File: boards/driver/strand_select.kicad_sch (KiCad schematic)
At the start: 16 parts, among them Q89 MMBT2222, Q90 MMBT2907, Q91 MMBT2222

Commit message: Driver: minor schematic cleanup and populated all of the BOM except for resistors
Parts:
- D158, D159, D160, D161, D162: MPN (none) -> 1N4148WS; Manufacturer (none) -> SMC Diode Solutions; Package (none) -> SOD-323; Rating (none) -> 300mA
- Q89, Q91: MPN (none) -> MMBT2222ALT1HTSA1; Manufacturer (none) -> Infineon Technologies; Package (none) -> SOT-23-3
- Q90: MPN (none) -> MMBT2907ALT1HTSA1; Manufacturer (none) -> Infineon Technologies; Package (none) -> SOT-23-3
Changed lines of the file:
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@@
+      (effects (font (size 1.27 1.27)) hide)
+    )
+    (property "MPN" "MMBT2907ALT1HTSA1" (id 6) (at 72.39 95.25 0)
+      (effects (font (size 1.27 1.27)) hide)
+    )
+    (property "Manufacturer" "Infineon Technologies" (id 7) (at 72.39 95.25 0)
+      (effects (font (size 1.27 1.27)) hide)
+    )
+    (property "Description" "TRANS PNP 60V 0.6A SOT23" (id 8) (at 72.39 95.25 0)
+      (effects (font (size 1.27 1.27)) hide)
+    )
+    (property "Package" "SOT-23-3" (id 9) (at 72.39 95.25 0)
       (effects (font (size 1.27 1.27)) hide)
     )
@@
       (effects (font (size 1.27 1.27)) hide)
     )
+    (property "MPN" "1N4148WS" (id 6) (at 74.93 86.36 0)
+      (effects (font (size 1.27 1.27)) hide)
+    )
+    (property "Manufacturer" "SMC Diode Solutions" (id 7) (at 74.93 86.36 0)
+      (effects (font (size 1.27 1.27)) hide)
+    )
+    (property "Description" "DIODE GEN PURP 75V 300MA SOD323" (id 8) (at 74.93 86.36 0)
+      (effects (font (size 1.27 1.27)) hide)
+    )
+    (property "Package" "SOD-323" (id 9) (at 74.93 86.36 0)
+      (effects (font (size 1.27 1.27)) hide)
+    )
+    (property "Rating" "300mA" (id 10) (at 74.93 86.36 0)
+      (effects (font (size 1.27 1.27)) hide)
+    )
     (pin "1")
     (pin "2")
@@
       (effects (font (size 1.27 1.27)) hide)
     )
+    (property "MPN" "1N4148WS" (id 6) (at 86.36 115.57 0)
+      (effects (font (size 1.27 1.27)) hide)
+    )
+    (property "Manufacturer" "SMC Diode Solutions" (id 7) (at 86.36 115.57 0)
+      (effects (font (size 1.27 1.27)) hide)
+    )
+    (property "Description" "DIODE GEN PURP 75V 300MA SOD323" (id 8) (at 86.36 115.57 0)
+      (effects (font (size 1.27 1.27)) hide)
+    )
+    (property "Package" "SOD-323" (id 9) (at 86.36 115.57 0)
+      (effects (font (size 1.27 1.27)) hide)
+    )
+    (property "Rating" "300mA" (id 10) (at 86.36 115.57 0)
+      (effects (font (size 1.27 1.27)) hide)
+    )
     (pin "1")
     (pin "2")
@@
       (effects (font (size 1.27 1.27)) hide)
     )
+    (property "MPN" "1N4148WS" (id 6) (at 86.36 121.92 0)
+      (effects (font (size 1.27 1.27)) hide)
+    )
+    (property "Manufacturer" "SMC Diode Solutions" (id 7) (at 86.36 121.92 0)
+      (effects (font (size 1.27 1.27)) hide)
+    )
+    (property "Description" "DIODE GEN PURP 75V 300MA SOD323" (id 8) (at 86.36 121.92 0)
+      (effects (font (size 1.27 1.27)) hide)
+    )
+    (property "Package" "SOD-323" (id 9) (at 86.36 121.92 0)
+      (effects (font (size 1.27 1.27)) hide)
+    )
+    (property "Rating" "300mA" (id 10) (at 86.36 121.92 0)
+      (effects (font (size 1.27 1.27)) hide)
+    )
     (pin "1")
     (pin "2")
@@
       (effects (font (size 1.27 1.27)) hide)
     )
+    (property "MPN" "1N4148WS" (id 6) (at 86.36 128.27 0)
+      (effects (font (size 1.27 1.27)) hide)
+    )
+    (property "Manufacturer" "SMC Diode Solutions" (id 7) (at 86.36 128.27 0)
+      (effects (font (size 1.27 1.27)) hide)
+    )
+    (property "Description" "DIODE GEN PURP 75V 300MA SOD323" (id 8) (at 86.36 128.27 0)
+      (effects (font (size 1.27 1.27)) hide)
+    )
+    (property "Package" "SOD-323" (id 9) (at 86.36 128.27 0)
+      (effects (font (size 1.27 1.27)) hide)
+    )
+    (property "Rating" "300mA" (id 10) (at 86.36 128.27 0)
+      (effects (font (size 1.27 1.27)) hide)
+    )
     (pin "1")
     (pin "2")
@@
     )
     (property "Part Number" "MMBT2222A-G" (id 5) (at 99.06 110.49 0)
+      (effects (font (size 1.27 1.27)) hide)
+    )
+    (property "MPN" "MMBT2222ALT1HTSA1" (id 6) (at 99.06 110.49 0)
+      (effects (font (size 1.27 1.27)) hide)
+    )
+    (property "Manufacturer" "Infineon Technologies" (id 7) (at 99.06 110.49 0)
+      (effects (font (size 1.27 1.27)) hide)
+    )
+    (property "Description" "TRANS NPN 40V 0.6A SOT-23" (id 8) (at 99.06 110.49 0)
+      (effects (font (size 1.27 1.27)) hide)
+    )
+    (property "Package" "SOT-23-3" (id 9) (at 99.06 110.49 0)
       (effects (font (size 1.27 1.27)) hide)
     )
@@
       (effects (font (size 1.27 1.27)) hide)
     )
+    (property "MPN" "MMBT2222ALT1HTSA1" (id 6) (at 49.53 116.84 0)
+      (effects (font (size 1.27 1.27)) hide)
+    )
+    (property "Manufacturer" "Infineon Technologies" (id 7) (at 49.53 116.84 0)
+      (effects (font (size 1.27 1.27)) hide)
+    )
+    (property "Description" "TRANS NPN 40V 0.6A SOT-23" (id 8) (at 49.53 116.84 0)
+      (effects (font (size 1.27 1.27)) hide)
+    )
+    (property "Package" "SOT-23-3" (id 9) (at 49.53 116.84 0)
+      (effects (font (size 1.27 1.27)) hide)
+    )
     (pin "1")
     (pin "2")
@@
       (effects (font (size 1.27 1.27)) hide)
     )
+    (property "MPN" "1N4148WS" (id 6) (at 52.07 127 0)
+      (effects (font (size 1.27 1.27)) hide)
+    )
+    (property "Manufacturer" "SMC Diode Solutions" (id 7) (at 52.07 127 0)
+      (effects (font (size 1.27 1.27)) hide)
+    )
+    (property "Description" "DIODE GEN PURP 75V 300MA SOD323" (id 8) (at 52.07 127 0)
+      (effects (font (size 1.27 1.27)) hide)
+    )
+    (property "Package" "SOD-323" (id 9) (at 52.07 127 0)
+      (effects (font (size 1.27 1.27)) hide)
+    )
+    (property "Rating" "300mA" (id 10) (at 52.07 127 0)
+      (effects (font (size 1.27 1.27)) hide)
+    )
     (pin "1")
     (pin "2")
@@
   (symbol (lib_id "power:GND") (at 52.07 132.08 0) (unit 1)
     (in_bom yes) (on_board yes)
-    (property "Reference" "#PWR0160" (id 0) (at 52.07 138.43 0)
+    (property "Reference" "#PWR0162" (id 0) (at 52.07 138.43 0)
       (effects (font (size 1.27 1.27)) hide)
     )
@@
   (symbol (lib_id "power:GND") (at 101.6 135.89 0) (unit 1)
     (in_bom yes) (on_board yes)
-    (property "Reference" "#PWR0161" (id 0) (at 101.6 142.24 0)
-      (effects (font (size 1.27 1.27)) hide)
-    )
+    (property "Reference" "#PWR0163" (id 0) (at 101.6 142.24 0)
+      (effects (font (size 1.27 1.27)) hide)
+    )

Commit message: Driver: filled out the rest of the BOM, except for defaults for nominal resistances
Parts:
- R268: MPN (none) -> ESR03EZPF1001; Manufacturer (none) -> Rohm Semiconductor; Package (none) -> 0603; Rating (none) -> 1/4W; Tolerance (none) -> 1%
- R269, R270, R272: MPN (none) -> ERJ-UP3F5101V; Manufacturer (none) -> Panasonic Electronic Components; Package (none) -> 0603; Rating (none) -> 1/4W; Tolerance (none) -> 1%
- R271: MPN (none) -> RCS0603680RFKEA; Manufacturer (none) -> Vishay Dale; Package (none) -> 0603; Rating (none) -> 1/4W; Tolerance (none) -> 1%
- R273: MPN (none) -> ERJ-PA3F3001V; Manufacturer (none) -> Panasonic Electronic Components; Package (none) -> 0603; Rating (none) -> 1/3W; Tolerance (none) -> 1%
- R274: MPN (none) -> ESR03EZPF10R0; Manufacturer (none) -> Rohm Semiconductor; Package (none) -> 0603; Rating (none) -> 1/4W; Tolerance (none) -> 1%
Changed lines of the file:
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@@
+      (effects (font (size 1.27 1.27)) hide)
+    )
+    (property "Description" "RES 5.1K OHM PULSE-WITHSTANDING 1% 1/4W 0603" (id 4) (at 59.69 100.33 0)
+      (effects (font (size 1.27 1.27)) hide)
+    )
+    (property "MPN" "ERJ-UP3F5101V" (id 5) (at 59.69 100.33 0)
+      (effects (font (size 1.27 1.27)) hide)
+    )
+    (property "Manufacturer" "Panasonic Electronic Components" (id 6) (at 59.69 100.33 0)
+      (effects (font (size 1.27 1.27)) hide)
+    )
+    (property "Package" "0603" (id 7) (at 59.69 100.33 0)
+      (effects (font (size 1.27 1.27)) hide)
+    )
+    (property "Rating" "1/4W" (id 8) (at 59.69 100.33 0)
+      (effects (font (size 1.27 1.27)) hide)
+    )
+    (property "Tolerance" "1%" (id 9) (at 59.69 100.33 0)
       (effects (font (size 1.27 1.27)) hide)
     )
@@
       (effects (font (size 1.27 1.27)) hide)
     )
+    (property "Description" "RES 5.1K OHM PULSE-WITHSTANDING 1% 1/4W 0603" (id 4) (at 59.69 88.9 0)
+      (effects (font (size 1.27 1.27)) hide)
+    )
+    (property "MPN" "ERJ-UP3F5101V" (id 5) (at 59.69 88.9 0)
+      (effects (font (size 1.27 1.27)) hide)
+    )
+    (property "Manufacturer" "Panasonic Electronic Components" (id 6) (at 59.69 88.9 0)
+      (effects (font (size 1.27 1.27)) hide)
+    )
+    (property "Package" "0603" (id 7) (at 59.69 88.9 0)
+      (effects (font (size 1.27 1.27)) hide)
+    )
+    (property "Rating" "1/4W" (id 8) (at 59.69 88.9 0)
+      (effects (font (size 1.27 1.27)) hide)
+    )
+    (property "Tolerance" "1%" (id 9) (at 59.69 88.9 0)
+      (effects (font (size 1.27 1.27)) hide)
+    )
     (pin "1")
     (pin "2")
@@
       (effects (font (size 1.27 1.27)) hide)
     )
+    (property "Description" "RES SMD 680 OHM PULSE-WITHSTANDING 1% 1/4W 0603" (id 4) (at 74.93 105.41 0)
+      (effects (font (size 1.27 1.27)) hide)
+    )
+    (property "MPN" "RCS0603680RFKEA" (id 5) (at 74.93 105.41 0)
+      (effects (font (size 1.27 1.27)) hide)
+    )
+    (property "Manufacturer" "Vishay Dale" (id 6) (at 74.93 105.41 0)
+      (effects (font (size 1.27 1.27)) hide)
+    )
+    (property "Package" "0603" (id 7) (at 74.93 105.41 0)
+      (effects (font (size 1.27 1.27)) hide)
+    )
+    (property "Rating" "1/4W" (id 8) (at 74.93 105.41 0)
+      (effects (font (size 1.27 1.27)) hide)
+    )
+    (property "Tolerance" "1%" (id 9) (at 74.93 105.41 0)
+      (effects (font (size 1.27 1.27)) hide)
+    )
     (pin "1")
     (pin "2")
@@
       (effects (font (size 1.27 1.27)) hide)
     )
+    (property "Description" "RES 5.1K OHM PULSE-WITHSTANDING 1% 1/4W 0603" (id 4) (at 74.93 119.38 0)
+      (effects (font (size 1.27 1.27)) hide)
+    )
+    (property "MPN" "ERJ-UP3F5101V" (id 5) (at 74.93 119.38 0)
+      (effects (font (size 1.27 1.27)) hide)
+    )
+    (property "Manufacturer" "Panasonic Electronic Components" (id 6) (at 74.93 119.38 0)
+      (effects (font (size 1.27 1.27)) hide)
+    )
+    (property "Package" "0603" (id 7) (at 74.93 119.38 0)
+      (effects (font (size 1.27 1.27)) hide)
+    )
+    (property "Rating" "1/4W" (id 8) (at 74.93 119.38 0)
+      (effects (font (size 1.27 1.27)) hide)
+    )
+    (property "Tolerance" "1%" (id 9) (at 74.93 119.38 0)
+      (effects (font (size 1.27 1.27)) hide)
+    )
     (pin "1")
     (pin "2")
@@
       (effects (font (size 1.27 1.27)) hide)
     )
+    (property "Description" "RES SMD 10 OHM PULSE-WITHSTANDING 1% 1/4W 0603" (id 4) (at 101.6 120.65 0)
+      (effects (font (size 1.27 1.27)) hide)
+    )
+    (property "MPN" "ESR03EZPF10R0" (id 5) (at 101.6 120.65 0)
+      (effects (font (size 1.27 1.27)) hide)
+    )
+    (property "Manufacturer" "Rohm Semiconductor" (id 6) (at 101.6 120.65 0)
+      (effects (font (size 1.27 1.27)) hide)
+    )
+    (property "Package" "0603" (id 7) (at 101.6 120.65 0)
+      (effects (font (size 1.27 1.27)) hide)
+    )
+    (property "Rating" "1/4W" (id 8) (at 101.6 120.65 0)
+      (effects (font (size 1.27 1.27)) hide)
+    )
+    (property "Tolerance" "1%" (id 9) (at 101.6 120.65 0)
+      (effects (font (size 1.27 1.27)) hide)
+    )
     (pin "1")
     (pin "2")
@@
     )
     (property "Datasheet" "~" (id 3) (at 101.6 90.17 0)
+      (effects (font (size 1.27 1.27)) hide)
+    )
+    (property "Rating" "1/3W" (id 4) (at 101.6 90.17 0)
+      (effects (font (size 1.27 1.27)) hide)
+    )
+    (property "Tolerance" "1%" (id 5) (at 101.6 90.17 0)
+      (effects (font (size 1.27 1.27)) hide)
+    )
+    (property "Description" "RES SMD 3K OHM PULSE-WITHSTANDING 1% 1/3W 0603" (id 6) (at 101.6 90.17 0)
+      (effects (font (size 1.27 1.27)) hide)
+    )
+    (property "MPN" "ERJ-PA3F3001V" (id 7) (at 101.6 90.17 0)
+      (effects (font (size 1.27 1.27)) hide)
+    )
+    (property "Manufacturer" "Panasonic Electronic Components" (id 8) (at 101.6 90.17 0)
+      (effects (font (size 1.27 1.27)) hide)
+    )
+    (property "Package" "0603" (id 9) (at 101.6 90.17 0)
       (effects (font (size 1.27 1.27)) hide)
     )
@@
       (effects (font (size 1.27 1.27)) hide)
     )
+    (property "Description" "RES SMD 1K OHM PULSE-WITHSTANDING 1% 1/4W 0603" (id 4) (at 39.37 116.84 0)
+      (effects (font (size 1.27 1.27)) hide)
+    )
+    (property "MPN" "ESR03EZPF1001" (id 5) (at 39.37 116.84 0)
+      (effects (font (size 1.27 1.27)) hide)
+    )
+    (property "Manufacturer" "Rohm Semiconductor" (id 6) (at 39.37 116.84 0)
+      (effects (font (size 1.27 1.27)) hide)
+    )
+    (property "Package" "0603" (id 7) (at 39.37 116.84 0)
+      (effects (font (size 1.27 1.27)) hide)
+    )
+    (property "Rating" "1/4W" (id 8) (at 39.37 116.84 0)
+      (effects (font (size 1.27 1.27)) hide)
+    )
+    (property "Tolerance" "1%" (id 9) (at 39.37 116.84 0)
+      (effects (font (size 1.27 1.27)) hide)
+    )

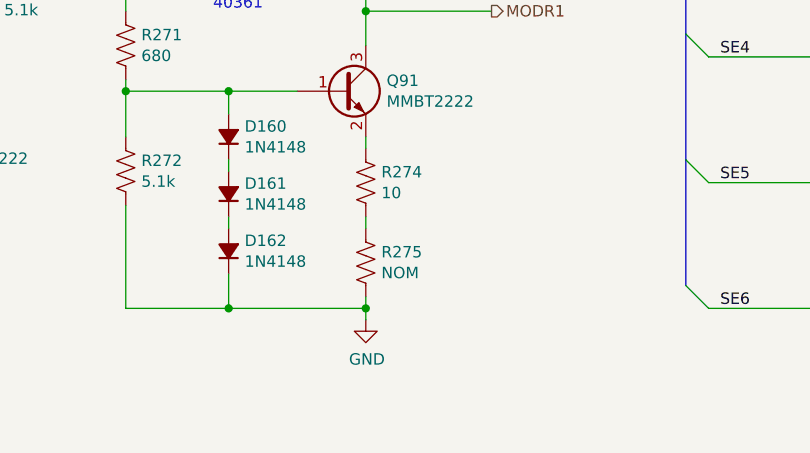
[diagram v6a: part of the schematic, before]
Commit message: Driver: completed the BOM and added some reference dimensions to the board layout
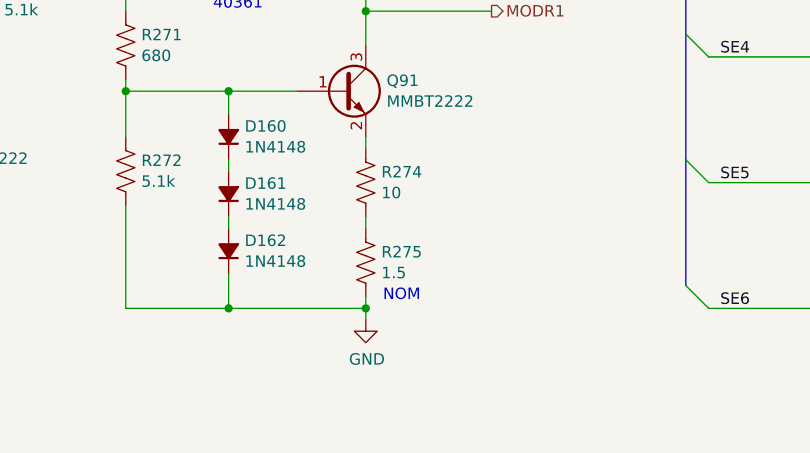
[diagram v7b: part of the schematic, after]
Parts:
- R275: value NOM -> 1.5; MPN (none) -> RCS06031R50FKEA; Manufacturer (none) -> Vishay Dale; Package (none) -> 0603; Rating (none) -> 1/4W; Tolerance (none) -> 1%
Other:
- note added: "NOM"
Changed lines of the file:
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@@
     (effects (font (size 1.27 1.27)) (justify right bottom))
+  )
+  (text "NOM" (at 103.505 133.985 0)
+    (effects (font (size 1.27 1.27)) (justify left bottom))
   )
   (text "40361" (at 90.17 101.6 180)
@@
       (effects (font (size 1.27 1.27)) (justify left))
     )
-    (property "Value" "NOM" (id 1) (at 103.3272 130.683 0)
+    (property "Value" "1.5" (id 1) (at 103.3272 130.683 0)
       (effects (font (size 1.27 1.27)) (justify left))
     )
@@
       (effects (font (size 1.27 1.27)) hide)
     )
+    (property "Description" "RES SMD 1.5 OHM PULSE-WITHSTANDING  1% 1/4W 0603" (id 4) (at 101.6 129.54 0)
+      (effects (font (size 1.27 1.27)) hide)
+    )
+    (property "MPN" "RCS06031R50FKEA" (id 5) (at 101.6 129.54 0)
+      (effects (font (size 1.27 1.27)) hide)
+    )
+    (property "Manufacturer" "Vishay Dale" (id 6) (at 101.6 129.54 0)
+      (effects (font (size 1.27 1.27)) hide)
+    )
+    (property "Package" "0603" (id 7) (at 101.6 129.54 0)
+      (effects (font (size 1.27 1.27)) hide)
+    )
+    (property "Rating" "1/4W" (id 8) (at 101.6 129.54 0)
+      (effects (font (size 1.27 1.27)) hide)
+    )
+    (property "Tolerance" "1%" (id 9) (at 101.6 129.54 0)
+      (effects (font (size 1.27 1.27)) hide)
+    )
